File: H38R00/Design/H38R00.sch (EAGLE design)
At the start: 72 parts, among them P1 HEXABIT_17.32_X2_POWER_ONLY, U1 LM5160DNT, U2 TPS65130RGERT, X1 INPUT, X2 OUT-15P, X3 OUT-15N, X4 OUT-5P

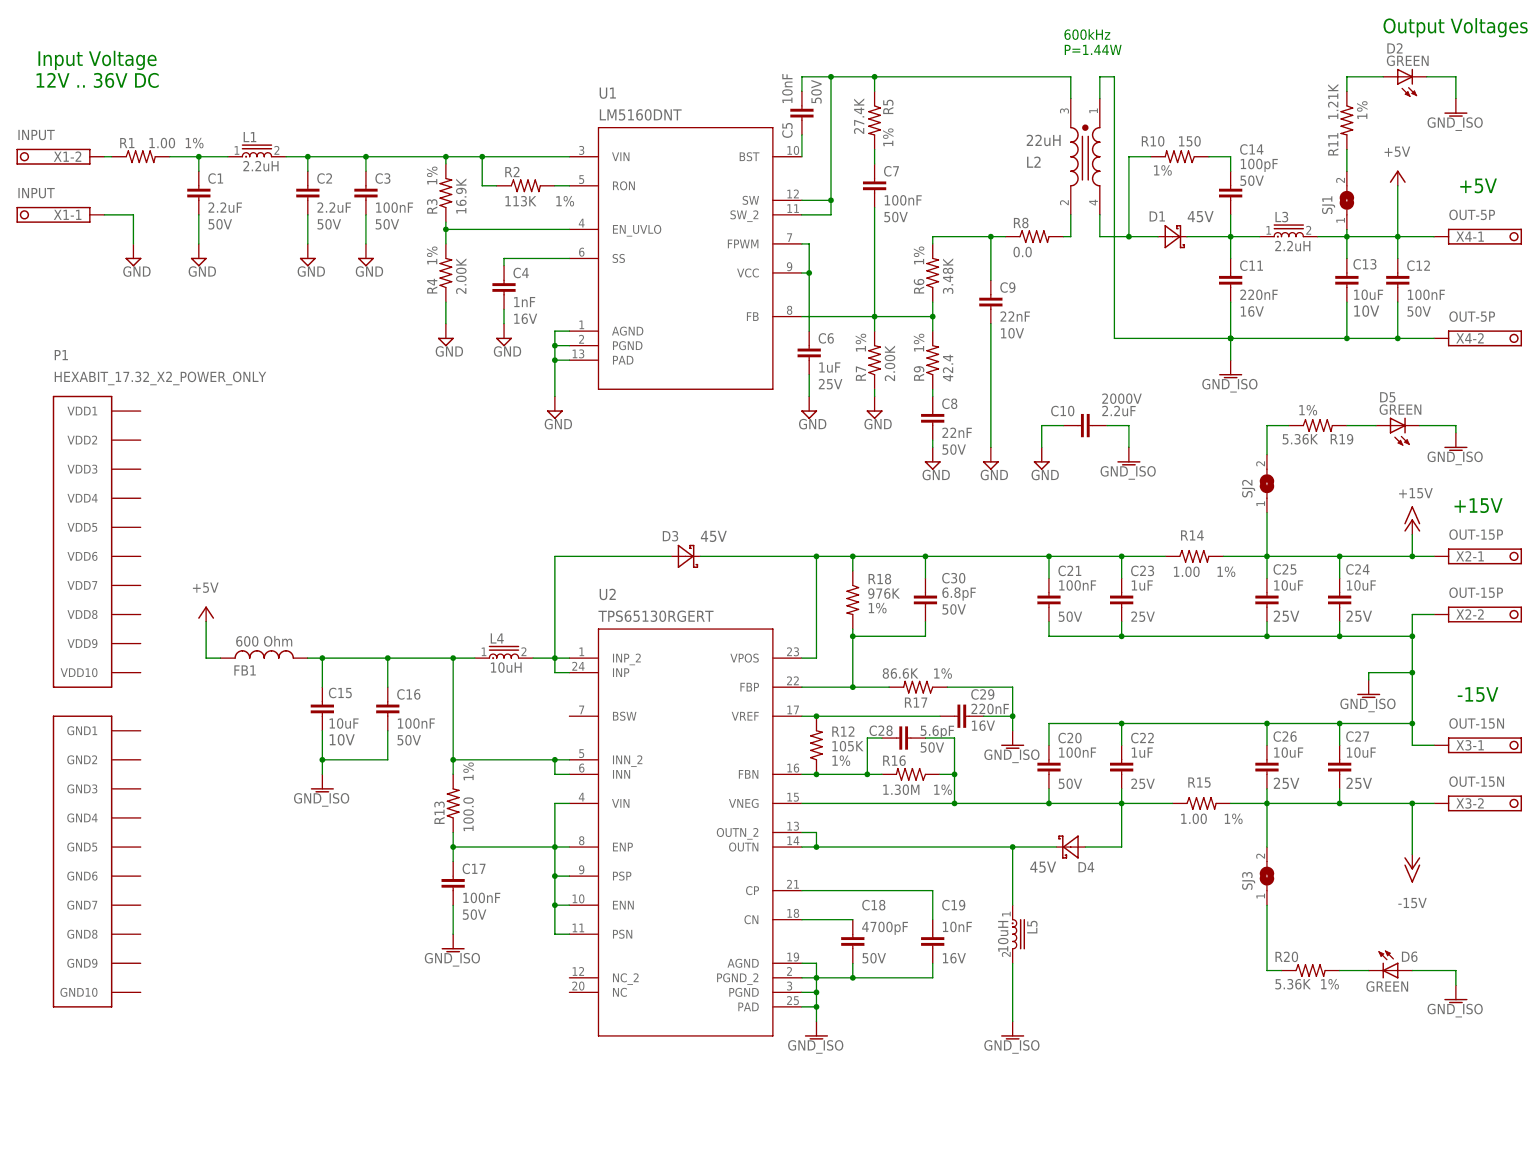
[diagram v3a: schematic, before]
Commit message: Renumber components Update transformer package Place connectors and half components
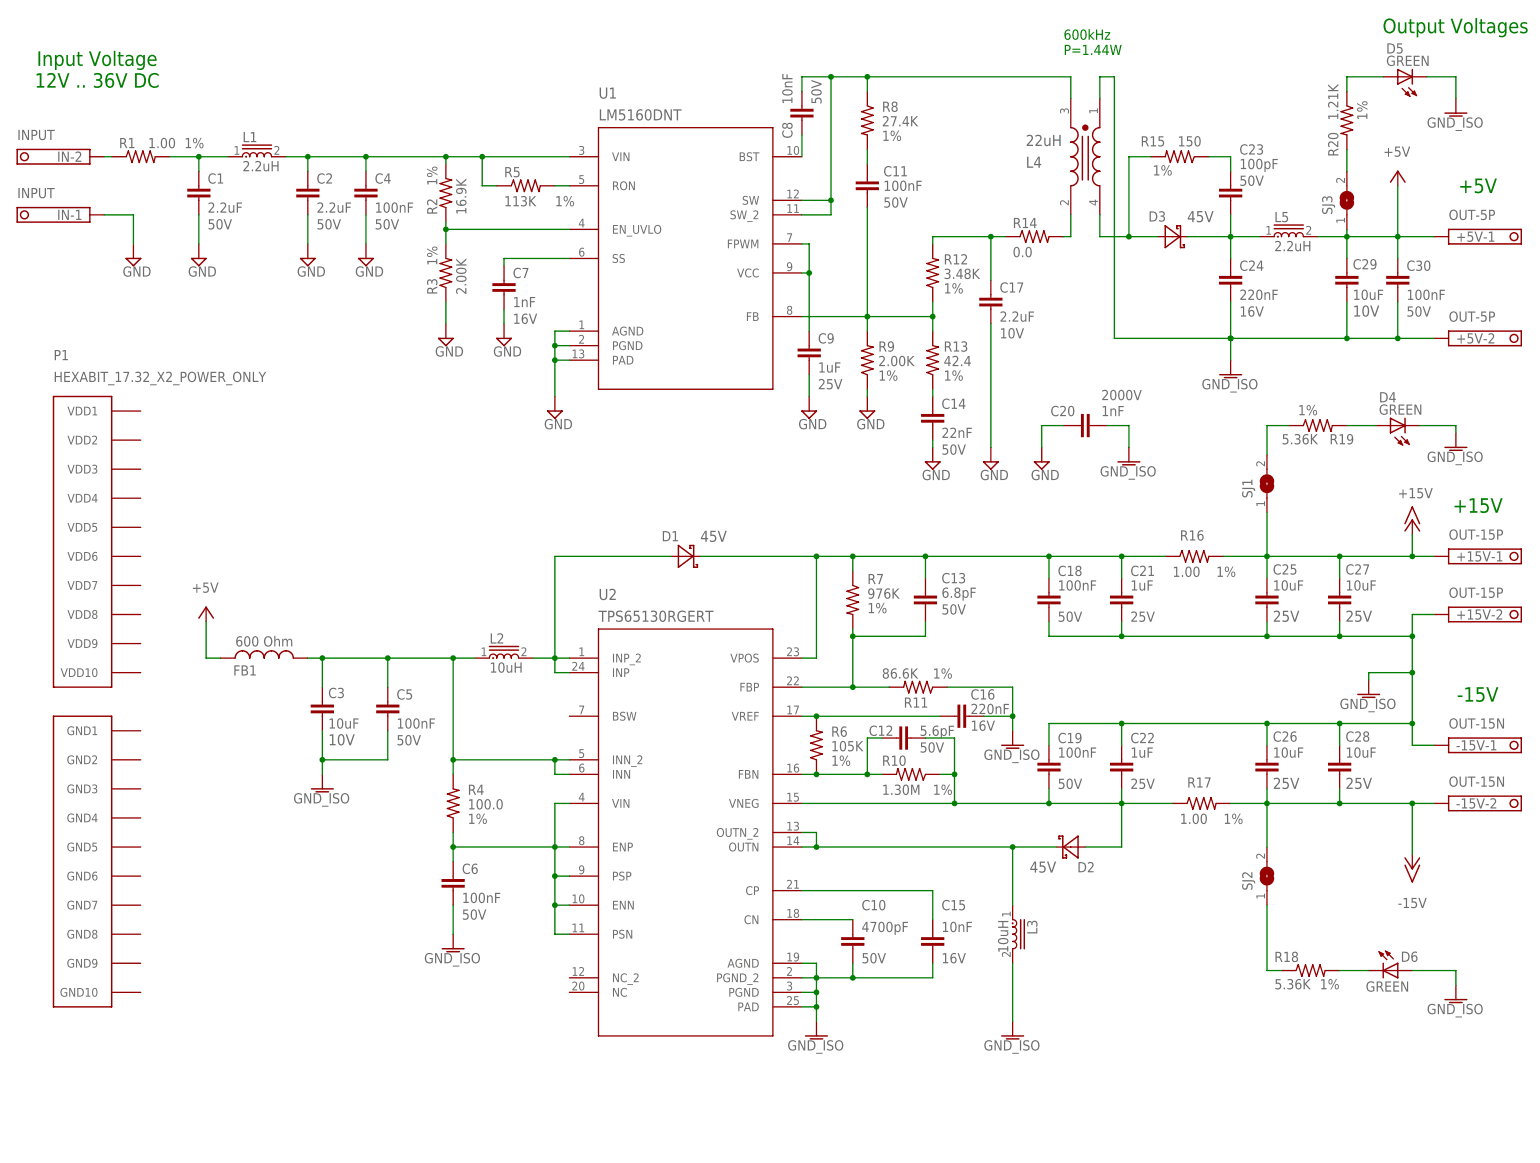
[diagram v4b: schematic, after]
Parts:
- C10: value 2.2uF -> 4700pF; device Hexabitz:C-1206 -> Hexabitz:C-0603; CAPACITANCE 1nF -> 4700pF; MFN Johanson -> Würth Elektronik; MPN 202R18W102KV4E -> 885012206087; OCTOPART_URL https://octopart.com/202r18w102kv4e-johanson-2172376?r=sp&s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 -> https://octopart.com/885012206087-w%C3%BCrth+elektronik-539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; TOLERANCE (none) -> 10%; VOLTAGE 2000V -> (none); VOLTAGE_RATING (none) -> 50V
- C11: value 220nF -> 100nF; CAPACITANCE 220nF -> 100nF; MFN Würth Elektronik -> TDK; MPN 885012206048 -> C1608X7R1H104K; OCTOPART_URL https://octopart.com/885012206048-w%C3%BCrth+elektronik-539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 -> https://octopart.com/c1608x7r1h104k080aa-tdk-25947665?r=sp&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; VOLTAGE_RATING 16V -> 50V
- C12: value 100nF -> 5.6pF; CAPACITANCE 100nF -> 5.6pF; MPN C1608X7R1H104K -> 06035A5R6CAT2A; OCTOPART_URL https://octopart.com/c1608x7r1h104k080aa-tdk-25947665?r=sp&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 -> https://octopart.com/06035a5r6cat2a-avx-194782?r=sp&s=arSRm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; TOLERANCE 10% -> 5%
- C13: value 10uF -> 6.8pF; device Hexabitz:C-0805 -> Hexabitz:C-0603; CAPACITANCE 10uF -> 6.8pF; MFN Würth Elektronik -> AVX; MPN 885012207026 -> 06035A6R8CAT2A; OCTOPART_URL (none) -> https://octopart.com/06035a6r8cat2a-avx-194783?r=sp&s=5-5NB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; OCTOPAR_URL https://octopart.com/885012207026-w%C3%BCrth+elektronik-654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 -> (none); VOLTAGE_RATING 10V -> 50V
- C14: value 100pF -> 22nF; CAPACITANCE 100pF -> 22nF; MFN KEMET -> Murata; MPN C0603C101J5GACTU -> GRM188R71H223KA01D; OCTOPART_URL https://octopart.com/c0603c101j5gactu-kemet-100052?r=sp&s=G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 -> https://octopart.com/grm188r71h223ka01d-murata-196232?r=sp&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; TOLERANCE 5% -> 10%
- C15: value 10uF -> 10nF; device Hexabitz:C-0805 -> Hexabitz:C-0603; CAPACITANCE 10uF -> 10nF; MPN 885012207026 -> 885012206040; OCTOPART_URL (none) -> https://octopart.com/885012206040-w%C3%BCrth+elektronik-539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; OCTOPAR_URL https://octopart.com/885012207026-w%C3%BCrth+elektronik-654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 -> (none); VOLTAGE_RATING 10V -> 16V
- C16: value 100nF -> 220nF; CAPACITANCE 100nF -> 220nF; MFN TDK -> Würth Elektronik; MPN C1608X7R1H104K -> 885012206048; OCTOPART_URL https://octopart.com/c1608x7r1h104k080aa-tdk-25947665?r=sp&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 -> https://octopart.com/885012206048-w%C3%BCrth+elektronik-539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; VOLTAGE_RATING 50V -> 16V
- C17: value 100nF -> 2.2uF; CAPACITANCE 100nF -> 2.2uF; MFN TDK -> Murata; MPN C1608X7R1H104K -> GRM188R71A225KE15D; OCTOPART_URL https://octopart.com/c1608x7r1h104k080aa-tdk-25947665?r=sp&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 -> https://octopart.com/grm188r71a225ke15d-murata-197889?r=sp&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; VOLTAGE_RATING 50V -> 10V
- C18: value 4700pF -> 100nF; CAPACITANCE 4700pF -> 100nF; MFN Würth Elektronik -> TDK; MPN 885012206087 -> C1608X7R1H104K; OCTOPART_URL https://octopart.com/885012206087-w%C3%BCrth+elektronik-539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 -> https://octopart.com/c1608x7r1h104k080aa-tdk-25947665?r=sp&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
- C19: value 10nF -> 100nF; CAPACITANCE 10nF -> 100nF; MFN Würth Elektronik -> TDK; MPN 885012206040 -> C1608X7R1H104K; OCTOPART_URL https://octopart.com/885012206040-w%C3%BCrth+elektronik-539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 -> https://octopart.com/c1608x7r1h104k080aa-tdk-25947665?r=sp&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; VOLTAGE_RATING 16V -> 50V
- C20: value 100nF -> 1nF; device Hexabitz:C-0603 -> Hexabitz:C-1206; CAPACITANCE 100nF -> 1nF; MFN TDK -> Johanson; MPN C1608X7R1H104K -> 202R18W102KV4E; OCTOPART_URL https://octopart.com/c1608x7r1h104k080aa-tdk-25947665?r=sp&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 -> https://octopart.com/202r18w102kv4e-johanson-2172376?r=sp&s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; TOLERANCE 10% -> (none); VOLTAGE (none) -> 2000V; VOLTAGE_RATING 50V -> (none)
- C21: value 100nF -> 1uF; CAPACITANCE 100nF -> 1uF; MFN TDK -> Taiyo Yuden; MPN C1608X7R1H104K -> TMK107B7105KA-T; OCTOPART_URL https://octopart.com/c1608x7r1h104k080aa-tdk-25947665?r=sp&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 -> https://octopart.com/tmk107b7105ka-t-taiyo+yuden-20363789?r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; VOLTAGE_RATING 50V -> 25V
- C23: value 1uF -> 100pF; CAPACITANCE 1uF -> 100pF; MFN Taiyo Yuden -> KEMET; MPN TMK107B7105KA-T -> C0603C101J5GACTU; OCTOPART_URL https://octopart.com/tmk107b7105ka-t-taiyo+yuden-20363789?r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 -> https://octopart.com/c0603c101j5gactu-kemet-100052?r=sp&s=G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; TOLERANCE 10% -> 5%; VOLTAGE_RATING 25V -> 50V
- C24: value 10uF -> 220nF; device Hexabitz:C-0805 -> Hexabitz:C-0603; CAPACITANCE 10uF -> 220nF; MFN Murata -> Würth Elektronik; MPN GRM21BC71E106KE11L -> 885012206048; OCTOPART_URL (none) -> https://octopart.com/885012206048-w%C3%BCrth+elektronik-539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; OCTOPAR_URL https://octopart.com/grm21bc71e106ke11l-murata-51454492?r=s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 -> (none); VOLTAGE_RATING 25V -> 16V
- C28: value 5.6pF -> 10uF; device Hexabitz:C-0603 -> Hexabitz:C-0805; CAPACITANCE 5.6pF -> 10uF; MFN TDK -> Murata; MPN 06035A5R6CAT2A -> GRM21BC71E106KE11L; OCTOPART_URL https://octopart.com/06035a5r6cat2a-avx-194782?r=sp&s=arSRm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 -> (none); OCTOPAR_URL (none) -> https://octopart.com/grm21bc71e106ke11l-murata-51454492?r=s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; TOLERANCE 5% -> 10%; VOLTAGE_RATING 50V -> 25V
- C29: value 220nF -> 10uF; device Hexabitz:C-0603 -> Hexabitz:C-0805; CAPACITANCE 220nF -> 10uF; MPN 885012206048 -> 885012207026; OCTOPART_URL https://octopart.com/885012206048-w%C3%BCrth+elektronik-539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 -> (none); OCTOPAR_URL (none) -> https://octopart.com/885012207026-w%C3%BCrth+elektronik-654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; VOLTAGE_RATING 16V -> 10V
- C3: value 100nF -> 10uF; device Hexabitz:C-0603 -> Hexabitz:C-0805; CAPACITANCE 100nF -> 10uF; MFN TDK -> Würth Elektronik; MPN C1608X7R1H104K -> 885012207026; OCTOPART_URL https://octopart.com/c1608x7r1h104k080aa-tdk-25947665?r=sp&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 -> (none); OCTOPAR_URL (none) -> https://octopart.com/885012207026-w%C3%BCrth+elektronik-654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; VOLTAGE_RATING 50V -> 10V
- C30: value 6.8pF -> 100nF; CAPACITANCE 6.8pF -> 100nF; MFN AVX -> TDK; MPN 06035A6R8CAT2A -> C1608X7R1H104K; OCTOPART_URL https://octopart.com/06035a6r8cat2a-avx-194783?r=sp&s=5-5NB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 -> https://octopart.com/c1608x7r1h104k080aa-tdk-25947665?r=sp&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
- C4: value 1nF -> 100nF; CAPACITANCE 1nF -> 100nF; MFN Würth Elektronik -> TDK; MPN 885012206034 -> C1608X7R1H104K; OCTOPART_URL https://octopart.com/885012206034-w%C3%BCrth+elektronik-539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 -> https://octopart.com/c1608x7r1h104k080aa-tdk-25947665?r=sp&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; VOLTAGE_RATING 16V -> 50V
- C5: value 10nF -> 100nF; CAPACITANCE 10nF -> 100nF; MFN KEMET -> TDK; MPN C0603C103J5RACTU -> C1608X7R1H104K; OCTOPART_URL https://octopart.com/c0603c103j5ractu-kemet-91371?r=sp&s=Ky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 -> https://octopart.com/c1608x7r1h104k080aa-tdk-25947665?r=sp&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
- C6: value 1uF -> 100nF; CAPACITANCE 1uF -> 100nF; MFN Taiyo Yuden -> TDK; MPN TMK107B7105KA-T -> C1608X7R1H104K; OCTOPART_URL https://octopart.com/tmk107b7105ka-t-taiyo+yuden-20363789?r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 -> https://octopart.com/c1608x7r1h104k080aa-tdk-25947665?r=sp&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; VOLTAGE_RATING 25V -> 50V
- C7: value 100nF -> 1nF; CAPACITANCE 100nF -> 1nF; MFN TDK -> Würth Elektronik; MPN C1608X7R1H104K -> 885012206034; OCTOPART_URL https://octopart.com/c1608x7r1h104k080aa-tdk-25947665?r=sp&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 -> https://octopart.com/885012206034-w%C3%BCrth+elektronik-539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; VOLTAGE_RATING 50V -> 16V
- C8: value 22nF -> 10nF; CAPACITANCE 22nF -> 10nF; MFN Murata -> KEMET; MPN GRM188R71H223KA01D -> C0603C103J5RACTU; OCTOPART_URL https://octopart.com/grm188r71h223ka01d-murata-196232?r=sp&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 -> https://octopart.com/c0603c103j5ractu-kemet-91371?r=sp&s=Ky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
- C9: value 22nF -> 1uF; CAPACITANCE 2.2uF -> 1uF; MFN Murata -> Taiyo Yuden; MPN GRM188R71A225KE15D -> TMK107B7105KA-T; OCTOPART_URL https://octopart.com/grm188r71a225ke15d-murata-197889?r=sp&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 -> https://octopart.com/tmk107b7105ka-t-taiyo+yuden-20363789?r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; VOLTAGE_RATING 10V -> 25V
- D2: value GREEN -> DIOD-SOD-123; device Hexabitz:VLMTG1300-GS08 -> Hexabitz:DIOD-SOD-123; CURRENT (none) -> 2A; MFN (none) -> ON Semiconductor; MPN (none) -> NTS245SFT1G; OCTOPART_URL (none) -> https://octopart.com/nts245sft1g-on+semiconductor-53638116?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; VOLTAGE_RATING_DC (none) -> 45V
- D4: value DIOD-SOD-123 -> GREEN; device Hexabitz:DIOD-SOD-123 -> Hexabitz:VLMTG1300-GS08; CURRENT 2A -> (none); MFN ON Semiconductor -> (none); MPN NTS245SFT1G -> (none); OCTOPART_URL https://octopart.com/nts245sft1g-on+semiconductor-53638116?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 -> (none); VOLTAGE_RATING_DC 45V -> (none)
- L2: value 22uH -> 10uH; device Hexabitz:WUERTH_ELEKTRONIK_74489430220WUERTH_ELEKTRONIK_74489430220_0_0 -> Hexabitz:WUERTH_ELEKTRONIK_74404024100WUERTH_ELEKTRONIK_74404024100_0_0
- L3: value 2.2uH -> 10uH; device Hexabitz:LQM18PN2R2MFHD -> Hexabitz:WUERTH_ELEKTRONIK_74404024100WUERTH_ELEKTRONIK_74404024100_0_0
- L4: value 10uH -> 22uH; device Hexabitz:WUERTH_ELEKTRONIK_74404024100WUERTH_ELEKTRONIK_74404024100_0_0 -> Hexabitz:WUERTH_ELEKTRONIK_74489430220WUERTH_ELEKTRONIK_74489430220_0_0
- L5: value 10uH -> 2.2uH; device Hexabitz:WUERTH_ELEKTRONIK_74404024100WUERTH_ELEKTRONIK_74404024100_0_0 -> Hexabitz:LQM18PN2R2MFHD
- R10: value 150 -> 1.30M; MPN CRCW0603150RFKEA -> CRCW06031M30FKEA; OCTOPART_URL https://octopart.com/crcw0603150rfkea-vishay-39455211?r=sp&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 -> https://octopart.com/crcw06031m30fkea-vishay-39601140?r=sp&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; RESISTANCE 150R -> 1.30M
- R11: value 1.21K -> 86.6K; MPN CRCW06031K21FKEA -> CRCW060386K6FKEA; OCTOPART_URL https://octopart.com/crcw06031k21fkea-vishay-39455541?r=sp&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 -> https://octopart.com/crcw060386k6fkea-vishay-39809057?r=sp&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; RESISTANCE 1.21K -> 86.6K
- R12: value 105K -> 3.48K; MPN CRCW0603105KFKEA -> CRCW06033K48FKEA; OCTOPART_URL https://octopart.com/crcw0603105kfkea-vishay-39783419?r=sp&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 -> https://octopart.com/crcw06033k48fkea-vishay-39806638?r=sp&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; RESISTANCE 105K -> 3.48K
- R13: value 100.0 -> 42.4; MPN CRCW0603100RFKEA -> CRCW060342R2FKEA; OCTOPART_URL https://octopart.com/crcw0603100rfkea-vishay-39454046?r=sp&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 -> https://octopart.com/crcw060342r2fkea-vishay-39808977?r=sp&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; RESISTANCE 100.0 -> 42.2R
- R14: value 1.00 -> 0.0; MFN Vishay-Dale -> Panasonic; MPN CRCW06031R00FKEA -> ERJ-3GEY0R00V; OCTOPART_URL https://octopart.com/crcw06031r00fkea-vishay-39713722?r=sp&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 -> https://octopart.com/erj-3gey0r00v-panasonic-55389238?r=sp&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; RESISTANCE 1.00 -> 0.0R; TOLERANCE 1% -> 5%
- R15: value 1.00 -> 150; MFN Vishay-Dale -> Vishay; MPN CRCW06031R00FKEA -> CRCW0603150RFKEA; OCTOPART_URL https://octopart.com/crcw06031r00fkea-vishay-39713722?r=sp&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 -> https://octopart.com/crcw0603150rfkea-vishay-39455211?r=sp&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; RESISTANCE 1.00 -> 150R
- R16: value 1.30M -> 1.00; MFN Vishay -> Vishay-Dale; MPN CRCW06031M30FKEA -> CRCW06031R00FKEA; OCTOPART_URL https://octopart.com/crcw06031m30fkea-vishay-39601140?r=sp&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 -> https://octopart.com/crcw06031r00fkea-vishay-39713722?r=sp&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; RESISTANCE 1.30M -> 1.00
- R17: value 86.6K -> 1.00; MFN Vishay -> Vishay-Dale; MPN CRCW060386K6FKEA -> CRCW06031R00FKEA; OCTOPART_URL https://octopart.com/crcw060386k6fkea-vishay-39809057?r=sp&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 -> https://octopart.com/crcw06031r00fkea-vishay-39713722?r=sp&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; RESISTANCE 86.6K -> 1.00
- R18: value 976K -> 5.36K; MPN CRCW0603976KFKEA -> CRCW06035K36FKEA; OCTOPART_URL https://octopart.com/crcw0603976kfkea-vishay-39847458?r=sp&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 -> https://octopart.com/crcw06035k36fkea-vishay-39850082?r=sp&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; RESISTANCE 976K -> 5.36K
- R2: value 113K -> 16.9K; MPN CRCW0603113KFKEA -> CRCW060316K9FKEA; OCTOPART_URL https://octopart.com/crcw0603113kfkea-vishay-39817257?r=sp&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 -> https://octopart.com/crcw060316k9fkea-vishay-39809405?r=sp&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; RESISTANCE 113K -> 16.9K
- R20: value 5.36K -> 1.21K; MPN CRCW06035K36FKEA -> CRCW06031K21FKEA; OCTOPART_URL https://octopart.com/crcw06035k36fkea-vishay-39850082?r=sp&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 -> https://octopart.com/crcw06031k21fkea-vishay-39455541?r=sp&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; RESISTANCE 5.36K -> 1.21K
- R3: value 16.9K -> 2.00K; MPN CRCW060316K9FKEA -> CRCW06032K00FKEA; OCTOPART_URL https://octopart.com/crcw060316k9fkea-vishay-39809405?r=sp&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 -> https://octopart.com/crcw06032k00fkea-vishay-39455515?r=sp&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; RESISTANCE 16.9K -> 2.00k
- R4: value 2.00K -> 100.0; MPN CRCW06032K00FKEA -> CRCW0603100RFKEA; OCTOPART_URL https://octopart.com/crcw06032k00fkea-vishay-39455515?r=sp&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 -> https://octopart.com/crcw0603100rfkea-vishay-39454046?r=sp&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; RESISTANCE 2.00k -> 100.0
- R5: value 27.4K -> 113K; MPN CRCW060327K4FKEA -> CRCW0603113KFKEA; OCTOPART_URL https://octopart.com/crcw060327k4fkea-vishay-40950191?r=sp&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 -> https://octopart.com/crcw0603113kfkea-vishay-39817257?r=sp&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; RESISTANCE 27.4K -> 113K
- R6: value 3.48K -> 105K; MPN CRCW06033K48FKEA -> CRCW0603105KFKEA; OCTOPART_URL https://octopart.com/crcw06033k48fkea-vishay-39806638?r=sp&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 -> https://octopart.com/crcw0603105kfkea-vishay-39783419?r=sp&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; RESISTANCE 3.48K -> 105K
- R7: value 2.00K -> 976K; MPN CRCW06032K00FKEA -> CRCW0603976KFKEA; OCTOPART_URL https://octopart.com/crcw06032k00fkea-vishay-39455515?r=sp&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 -> https://octopart.com/crcw0603976kfkea-vishay-39847458?r=sp&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; RESISTANCE 2.00k -> 976K
- R8: value 0.0 -> 27.4K; MFN Panasonic -> Vishay; MPN ERJ-3GEY0R00V -> CRCW060327K4FKEA; OCTOPART_URL https://octopart.com/erj-3gey0r00v-panasonic-55389238?r=sp&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 -> https://octopart.com/crcw060327k4fkea-vishay-40950191?r=sp&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; RESISTANCE 0.0R -> 27.4K; TOLERANCE 5% -> 1%
- R9: value 42.4 -> 2.00K; MPN CRCW060342R2FKEA -> CRCW06032K00FKEA; OCTOPART_URL https://octopart.com/crcw060342r2fkea-vishay-39808977?r=sp&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 -> https://octopart.com/crcw06032k00fkea-vishay-39455515?r=sp&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; RESISTANCE 42.2R -> 2.00k
- renumbered X1 to IN, X2 to +15V, X3 to -15V, X4 to +5V
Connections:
- net +15V: now also C27.1, R16.2, SJ1.1; no longer C24.1, R14.2, SJ2.1
- net +5V: now also C29.1, C30.1, L5.2, SJ3.1; no longer C12.1, C13.1, L3.2, SJ1.1
- net -15V: now also C28.2, R17.2, SJ2.2; no longer C27.2, R15.2, SJ3.2
- net AGND: now also C19.1, C20.2, C27.2, C28.1, C3.2, C30.2, C5.2, C6.2, D4.C, L3.2, L4.1, R11.1; no longer C11.2, C12.2, C13.2, C17.2, C19.2, C20.1, C23.2, C27.1, D2.C, L2.1, L5.2, R17.1
- net GND: now also C14.2, C17.2, C20.1, C7.2, R3.1, R9.1; no longer C10.1, C3.2, C6.2, C8.2, R4.1, R7.1
- net N$10: now also C11.2, R12.1, R13.2; no longer C7.2, R6.1, R7.2
- net N$11: now also C11.1, R8.2; no longer C7.1, R5.2
- net N$12: now also C17.1, R12.2, R14.1; no longer C9.1, R6.2, R8.1
- net N$13: now also L4.2, R14.2; no longer L2.2, R8.2
- net N$14: now also C14.1, R13.1; no longer C8.1, R9.1
- net N$15: now also C23.2, C24.1, D3.C, L5.1; no longer C11.1, C14.2, D1.C, L3.1
- net N$16: now also D3.A, L4.4, R15.2; no longer D1.A, L2.4, R10.2
- net N$17: now also C23.1, R15.1; no longer C14.1, R10.1
- net N$18: now also C3.1, C5.1, L2.1, R4.2; no longer C15.1, C16.1, L4.1, R13.2
- net N$19: now also R20.2, SJ3.2; no longer R11.2, SJ1.2
- net N$20: now also D5.A, R20.1; no longer D2.A, R11.1
- net N$21: now also D1.A, L2.2; no longer D3.A, L4.2
- net N$22: now also C13.2, C18.1, D1.C, R16.1, R7.1; no longer C23.1, C30.2, D3.C, R14.1, R18.1
- net N$23: now also C6.1, R4.1; no longer C17.1, R13.1
- net N$24: now also C10.1; no longer C18.1
- net N$25: now also C15.1; no longer C19.1
- net N$26: now also D2.C, L3.1; no longer D4.C, L5.1
- net N$27: now also C12.2, C19.2, D2.A, R10.1, R17.1; no longer C20.2, C28.2, D4.A, R15.1, R16.1
- net N$28: now also C12.1, R10.2, R6.1; no longer C28.1, R12.1, R16.2
- net N$29: now also C16.1, R6.2; no longer C29.1, R12.2
- net N$3: now also C4.1, R2.2, R5.1; no longer C3.1, R2.1, R3.2
- net N$30: now also C13.1, R11.2, R7.2; no longer C30.1, R17.2, R18.2
- net N$31: now also SJ1.2; no longer SJ2.2
- net N$32: now also D4.A; no longer D5.A
- net N$33: now also R18.1, SJ2.1; no longer R20.1, SJ3.1
- net N$34: now also R18.2; no longer R20.2
- net N$4: now also R5.2; no longer R2.2
- net N$5: now also R2.1, R3.2; no longer R3.1, R4.2
- net N$6: now also C7.1; no longer C4.1
- net N$7: now also C8.2, L4.3, R8.1; no longer C5.2, L2.3, R5.1
- net N$8: now also C8.1; no longer C5.1
- net N$9: now also C9.1; no longer C6.1
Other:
- moved on the sheet: C10, C11, C12, C13, C14, C15, C16, C17, C18, C19, C20, C21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

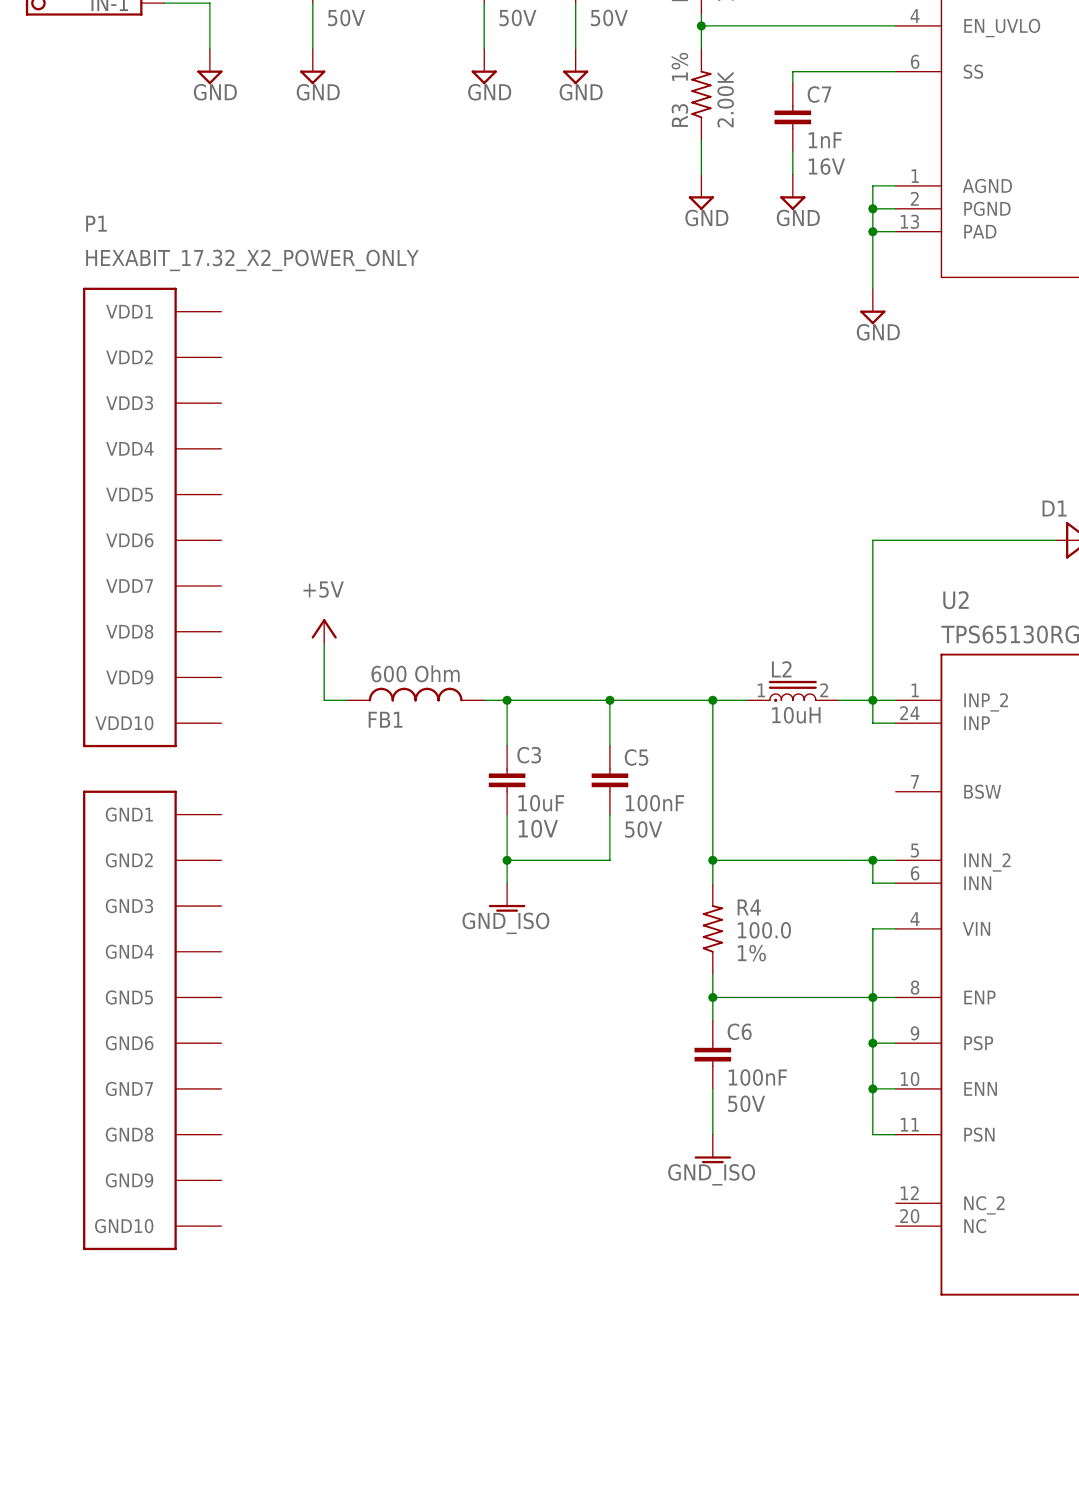
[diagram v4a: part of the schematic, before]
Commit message: added 3.3V LDO on 5V output
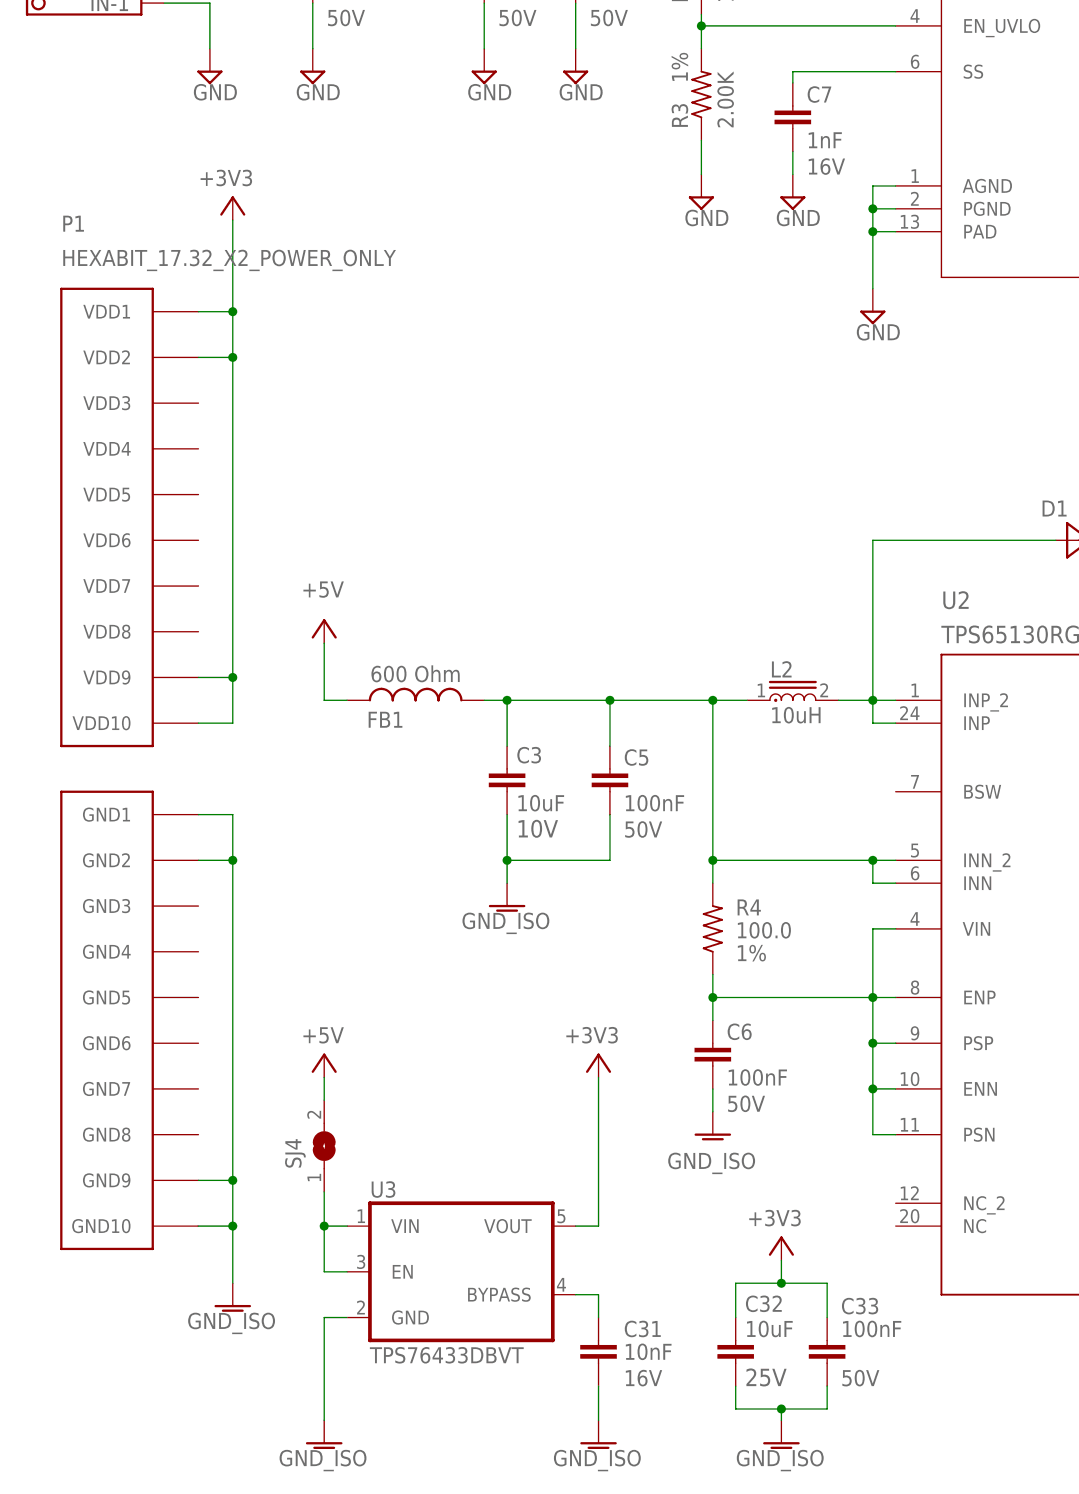
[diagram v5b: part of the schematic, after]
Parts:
- added C31: 10nF, Hexabitz:C-0603
- added C32: 10uF, Hexabitz:C-0805
- added C33: 100nF, Hexabitz:C-0603
- added SJ4: (no value), jumper:SJ
- added U3: TPS76433DBVT, Hexabitz:TPS76433DBVT
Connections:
- new net +3V3: C32.1, C33.1, P1.VDD1, P1.VDD10, P1.VDD2, P1.VDD9, U3.VOUT
- new net N$35: C31.1, U3.BYPASS
- new net N$36: SJ4.1, U3.EN, U3.VIN
- net +5V: now also SJ4.2
- net AGND: now also C31.2, C32.2, C33.2, P1.GND1, P1.GND10, P1.GND2, P1.GND9, U3.GND
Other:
- moved on the sheet: P1
